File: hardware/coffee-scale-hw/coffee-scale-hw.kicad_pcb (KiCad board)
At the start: 2 copper layers, 60 x 35 mm, 63 parts, among them J1 PWR_IN, J2 OLED, J3 LOAD_CELL, Q1 AO3401A, Q2 AO3401A, Q3 PNP, SW1 SW_SPDT, SW2 SW_BACK, SW3 SW_L, SW4 SW_R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

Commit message: Working on HW design
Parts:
- moved J3 18.2 mm to (168.8, 80.0)
- moved R18 16.8 mm to (172.8, 88.2), turned to 90 degrees
- moved R19 14.8 mm to (170.8, 88.2), turned to 90 degrees
- moved JP1 14.6 mm to (156.2, 98.0)
- moved C17 14.0 mm to (174.5, 94.8), turned to 90 degrees
- moved L2 13.7 mm to (163.0, 86.5), turned to -90 degrees
- moved R16 13.3 mm to (168.8, 88.2), turned to 90 degrees
- moved C14 13.1 mm to (171.8, 91.0), turned to 180 degrees
- moved R17 12.2 mm to (166.8, 88.2), turned to -90 degrees
- moved R20 11.9 mm to (160.0, 98.0)
- moved Q3 10.7 mm to (163.8, 90.2)
- moved C6 10.2 mm to (175.8, 104.2)
- moved C8 10.2 mm to (166.8, 107.8)
- moved L1 10.2 mm to (176.8, 109.2)
- moved R5 10.2 mm to (166.8, 110.2)
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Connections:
- J1 pad 1: Net-(J1-Pin_1) -> GND
- J1 pad 2: GND -> Net-(J1-Pin_2)
- SW1 pad 2: Net-(J1-Pin_1) -> Net-(J1-Pin_2)
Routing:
- net Net-(Q3-C): track 0.00 -> 11.5 mm
- net Net-(JP1-A): track 0.00 -> 9.84 mm
- net HX711_E+: track 0.00 -> 8.70 mm
- net Net-(U3-VBG): track 0.00 -> 6.55 mm
- net Net-(U3-VFB): track 0.00 -> 6.51 mm
- net HX711_A-: track 0.00 -> 5.54 mm
- net HX711_A+: track 0.00 -> 5.54 mm
- net Net-(U3-INA+): track 0.00 -> 4.63 mm
- net Net-(U3-INA-): track 0.00 -> 4.45 mm
- net Net-(Q3-B): track 0.00 -> 2.37 mm
- added copper zone on B.Cu, net +5V

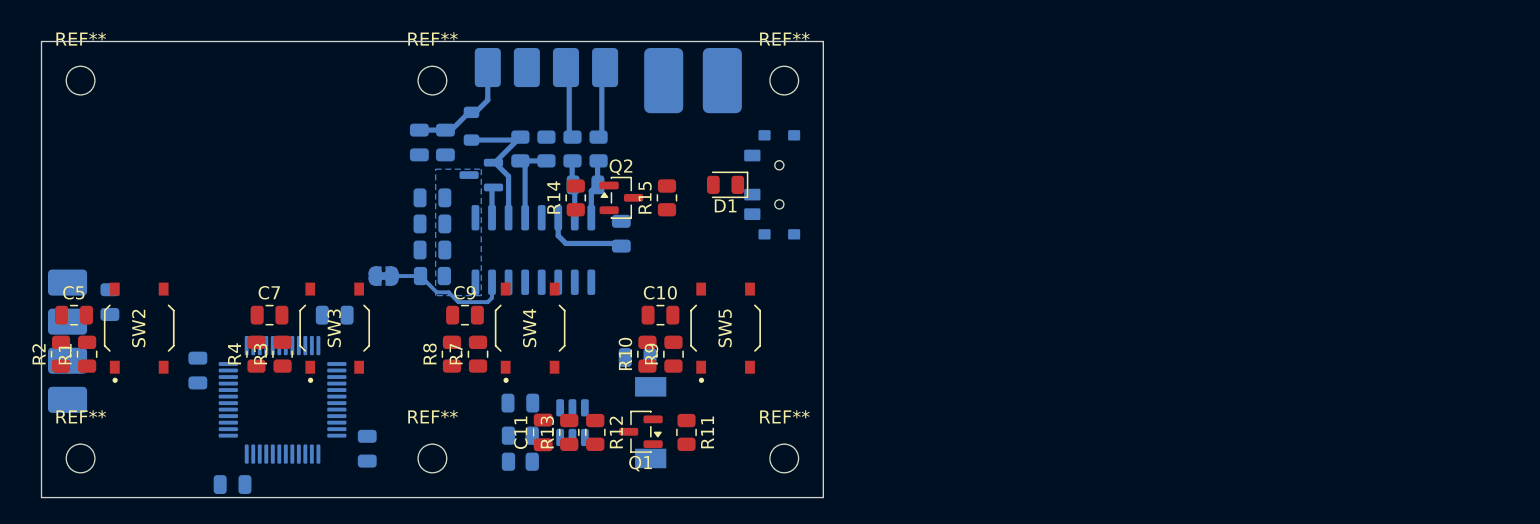
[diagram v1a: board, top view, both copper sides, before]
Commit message: Improved hx711 init
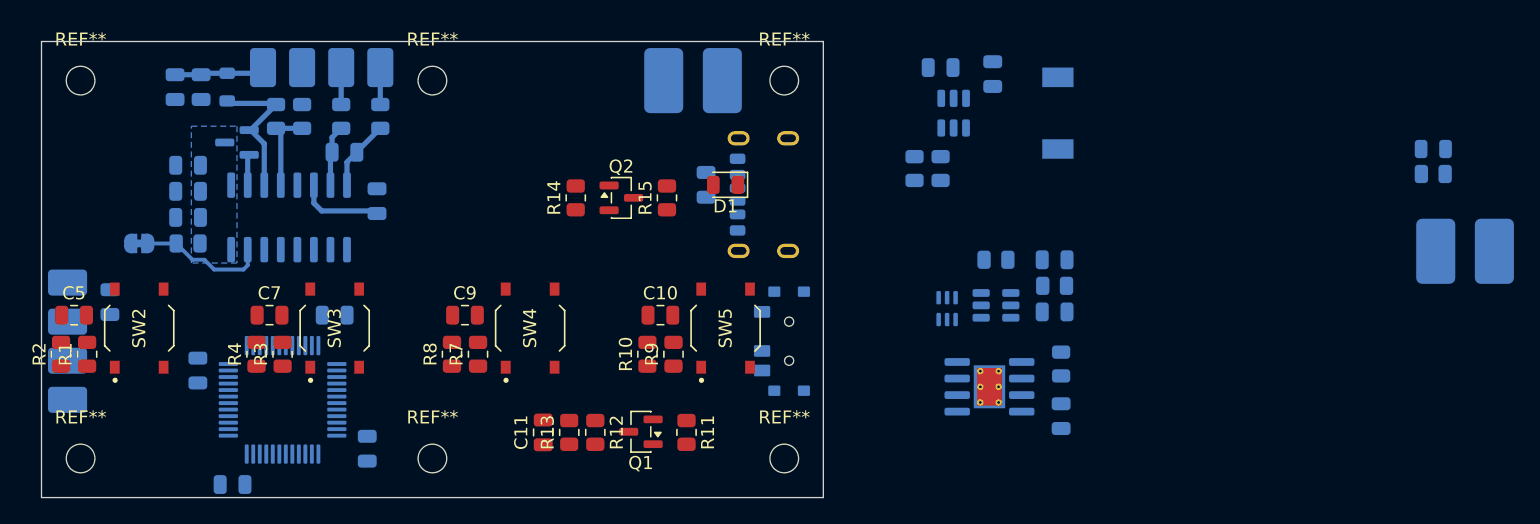
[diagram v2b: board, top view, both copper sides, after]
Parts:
- added C20: 10u, Capacitor_SMD:C_0805_2012Metric, B.Cu at (207.8, 96.8)
- added C21: 100n, Capacitor_SMD:C_0805_2012Metric, B.Cu at (207.8, 100.8)
- added C22: 100n, Capacitor_SMD:C_0805_2012Metric, B.Cu at (181.0, 91.0)
- added C23: 100n, Capacitor_SMD:C_0805_2012Metric, B.Cu at (208.2, 108.8)
- added D2: LED_CHRG, LED_SMD:LED_0805_2012Metric, B.Cu at (236.8, 88.2)
- added J4: BAT_IN, MyFootprints:Terminal_Pad_01x02-3x5mm, B.Cu at (239.2, 93.1)
- added J5: USB_C_Receptacle_PowerOnly_24P, Connector_USB:USB_C_Receptacle_GCT_USB4125-xx-x_6P_TopMnt_Horizontal, B.Cu at (186.5, 91.8)
- added Q4: Q_Dual_NMOS_S1G1D2S2G2D1, Package_TO_SOT_SMD:SOT-363_SC-70-6, B.Cu at (199.5, 100.5)
- added R21: 100R, Resistor_SMD:R_0805_2012Metric, B.Cu at (207.8, 98.8)
- added R22: 1k, Resistor_SMD:R_0805_2012Metric, B.Cu at (203.2, 96.8)
- added R23: 1k, Resistor_SMD:R_0805_2012Metric, B.Cu at (236.8, 90.2)
- added R24: 1k2, Resistor_SMD:R_0805_2012Metric, B.Cu at (208.2, 104.8)
- added U4: DW01A, Package_TO_SOT_SMD:SOT-23-6, B.Cu at (203.2, 100.2)
- added U5: TP4056-42-ESOP8, Package_SO:SOIC-8-1EP_3.9x4.9mm_P1.27mm_EP2.41x3.3mm_ThermalVias, B.Cu at (202.8, 106.5)
- C6: value C_Small -> ?
- SW1: value SW_SPDT -> SW_PWR
- moved C8 41.3 mm to (199.0, 82.0)
- moved R6 39.3 mm to (199.0, 89.8), turned to -90 degrees
- moved L1 39.3 mm to (208.0, 85.5)
- moved U1 37.7 mm to (200.0, 85.5)
- moved R5 36.5 mm to (197.0, 89.8), turned to 90 degrees
- moved C6 34.9 mm to (203.0, 82.5), turned to 90 degrees
- moved C12 19.2 mm to (142.2, 83.5)
- moved C13 19.2 mm to (140.2, 83.5)
- moved L2 19.0 mm to (144.2, 83.5)
- moved C16 18.9 mm to (141.2, 89.5)
- moved C17 18.9 mm to (155.8, 92.2)
- moved C18 18.9 mm to (141.2, 91.5)
- moved C19 18.9 mm to (141.2, 93.5)
- moved JP1 18.9 mm to (137.5, 95.5)
- moved Q3 18.9 mm to (145.0, 87.8)
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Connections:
- J1 pad 2: Net-(J1-Pin_2) -> +BATT
- SW1 pad 1: unconnected-(SW1-A-Pad1) -> +5V
- SW1 pad 2: Net-(J1-Pin_2) -> Net-(SW1-B)
- SW1 pad 3: +BATT -> GND
- U1 pad 4: +5V -> Net-(SW1-B)
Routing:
- net HX711_A-: track 5.54 -> 2.84 mm
- net HX711_A+: track 5.54 -> 2.84 mm
- net HX711_E+: track 8.70 -> 6.98 mm
- net Net-(U3-INA+): track 4.63 -> 5.42 mm

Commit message: Added LiPo battery USB-C charger
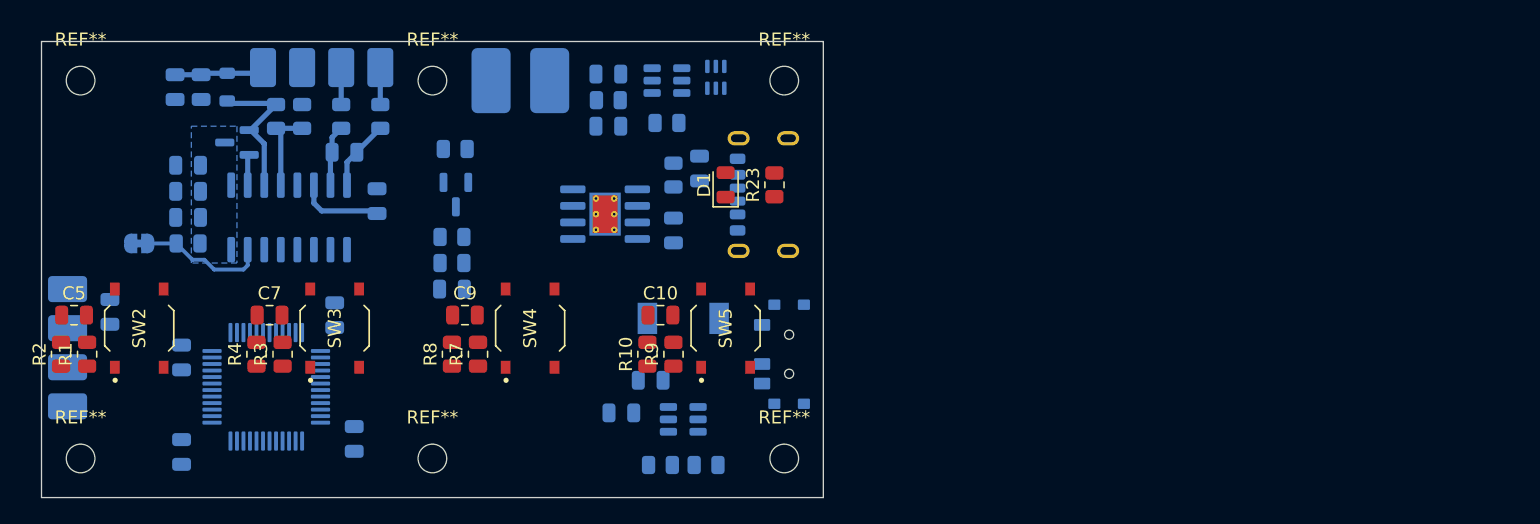
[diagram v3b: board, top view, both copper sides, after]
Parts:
- removed the D1 at (182.5, 91.0)
- removed J4: BAT_IN, MyFootprints:Terminal_Pad_01x02-3x5mm
- removed Q2: AO3401A, Package_TO_SOT_SMD:SOT-23
- removed R14: 10k, Resistor_SMD:R_0805_2012Metric
- removed R15: 2k, Resistor_SMD:R_0805_2012Metric
- C11, Q1, R11, R12, R13: moved to B.Cu
- D1: renamed from D2; moved to F.Cu
- J1: value PWR_IN -> BAT_IN
- R23: moved to F.Cu
- moved D1 54.4 mm to (182.5, 91.0), turned to 90 degrees
- moved R23 50.6 mm to (186.2, 91.0), turned to 90 degrees
- moved C21 38.8 mm to (173.5, 82.5), turned to 180 degrees
- moved R21 37.1 mm to (173.5, 84.5), turned to 180 degrees
- moved C8 36.1 mm to (174.5, 108.5)
- moved C20 35.8 mm to (173.5, 86.5), turned to 0 degrees
- moved C6 35.2 mm to (176.8, 106.0), turned to 180 degrees
- moved R24 33.1 mm to (178.5, 90.2)
- moved C23 33.0 mm to (178.5, 94.5)
- moved L1 32.8 mm to (179.2, 101.2), turned to 0 degrees
- moved U5 32.3 mm to (173.2, 93.2)
- moved U1 31.3 mm to (179.2, 109.0), turned to 180 degrees
- moved U4 30.6 mm to (178.0, 83.0), turned to 180 degrees
- moved R5 30.0 mm to (177.5, 112.5), turned to 0 degrees
- moved R6 29.0 mm to (181.0, 112.5), turned to 0 degrees
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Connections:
- C21 pad 2: Net-(J4-Pin_2) -> Net-(J1-Pin_2)
- J1 pad 1: GND -> +BATT
- J1 pad 2: +BATT -> Net-(J1-Pin_2)
- Q4 pad 4: Net-(J4-Pin_2) -> Net-(J1-Pin_2)
- U4 pad 6: Net-(J4-Pin_2) -> Net-(J1-Pin_2)
